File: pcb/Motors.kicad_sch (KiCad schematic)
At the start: 10 parts, among them M1 LEFT, M2 RIGHT, U11 TB6612FNG

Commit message: [pcb] Test points reduced to 1.5mm; flow control series resistors added
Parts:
- TP14, TP15: footprint TestPoint:TestPoint_Pad_D2.0mm -> TestPoint:TestPoint_Pad_D1.5mm
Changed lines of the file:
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@@
       (effects (font (size 1.27 1.27)) (justify left) hide)
     )
-    (property "Footprint" "TestPoint:TestPoint_Pad_D2.0mm" (at 30.48 68.58 0)
+    (property "Footprint" "TestPoint:TestPoint_Pad_D1.5mm" (at 30.48 68.58 0)
       (effects (font (size 1.27 1.27)) hide)
     )
@@
       (effects (font (size 1.27 1.27)) (justify left) hide)
     )
-    (property "Footprint" "TestPoint:TestPoint_Pad_D2.0mm" (at 40.64 63.5 0)
+    (property "Footprint" "TestPoint:TestPoint_Pad_D1.5mm" (at 40.64 63.5 0)
       (effects (font (size 1.27 1.27)) hide)
     )
@@
   (symbol (lib_id "power:+3.3V") (at 46.99 58.42 0) (unit 1)
     (in_bom yes) (on_board yes) (dnp no) (fields_autoplaced)
-    (property "Reference" "#PWR041" (at 46.99 62.23 0)
+    (property "Reference" "#PWR054" (at 46.99 62.23 0)
       (effects (font (size 1.27 1.27)) hide)
     )
@@
       (project "Autko"
         (path "/8d5cfdec-de34-4148-9100-7125640c46f5/541574ca-21e4-445f-b8e2-ded2c59d3b8a"
-          (reference "#PWR041") (unit 1)
+          (reference "#PWR054") (unit 1)
         )
       )
@@
   (symbol (lib_id "power:GND") (at 90.17 44.45 0) (unit 1)
     (in_bom yes) (on_board yes) (dnp no)
-    (property "Reference" "#PWR040" (at 90.17 50.8 0)
+    (property "Reference" "#PWR053" (at 90.17 50.8 0)
       (effects (font (size 1.27 1.27)) hide)
     )
@@
       (project "Autko"
         (path "/8d5cfdec-de34-4148-9100-7125640c46f5/541574ca-21e4-445f-b8e2-ded2c59d3b8a"
-          (reference "#PWR040") (unit 1)
+          (reference "#PWR053") (unit 1)
         )
       )
@@
   (symbol (lib_id "power:+3.3V") (at 46.99 31.75 0) (unit 1)
     (in_bom yes) (on_board yes) (dnp no) (fields_autoplaced)
-    (property "Reference" "#PWR037" (at 46.99 35.56 0)
+    (property "Reference" "#PWR050" (at 46.99 35.56 0)
       (effects (font (size 1.27 1.27)) hide)
     )
@@
       (project "Autko"
         (path "/8d5cfdec-de34-4148-9100-7125640c46f5/541574ca-21e4-445f-b8e2-ded2c59d3b8a"
-          (reference "#PWR037") (unit 1)
+          (reference "#PWR050") (unit 1)
         )
       )
@@
   (symbol (lib_id "power:+7.5V") (at 90.17 31.75 0) (unit 1)
     (in_bom yes) (on_board yes) (dnp no) (fields_autoplaced)
-    (property "Reference" "#PWR038" (at 90.17 35.56 0)
+    (property "Reference" "#PWR051" (at 90.17 35.56 0)
       (effects (font (size 1.27 1.27)) hide)
     )
@@
       (project "Autko"
         (path "/8d5cfdec-de34-4148-9100-7125640c46f5/541574ca-21e4-445f-b8e2-ded2c59d3b8a"
-          (reference "#PWR038") (unit 1)
+          (reference "#PWR051") (unit 1)
         )
       )
@@
   (symbol (lib_id "power:GND") (at 46.99 44.45 0) (unit 1)
     (in_bom yes) (on_board yes) (dnp no)
-    (property "Reference" "#PWR039" (at 46.99 50.8 0)
+    (property "Reference" "#PWR052" (at 46.99 50.8 0)
       (effects (font (size 1.27 1.27)) hide)
     )
@@
       (project "Autko"
         (path "/8d5cfdec-de34-4148-9100-7125640c46f5/541574ca-21e4-445f-b8e2-ded2c59d3b8a"
-          (reference "#PWR039") (unit 1)
+          (reference "#PWR052") (unit 1)
         )
       )
@@
   (symbol (lib_id "power:GND") (at 67.31 97.79 0) (unit 1)
     (in_bom yes) (on_board yes) (dnp no)
-    (property "Reference" "#PWR042" (at 67.31 104.14 0)
+    (property "Reference" "#PWR055" (at 67.31 104.14 0)
       (effects (font (size 1.27 1.27)) hide)
     )
@@
       (project "Autko"
         (path "/8d5cfdec-de34-4148-9100-7125640c46f5/541574ca-21e4-445f-b8e2-ded2c59d3b8a"
-          (reference "#PWR042") (unit 1)
-        )
-      )
+          (reference "#PWR055") (unit 1)
+        )
+      )

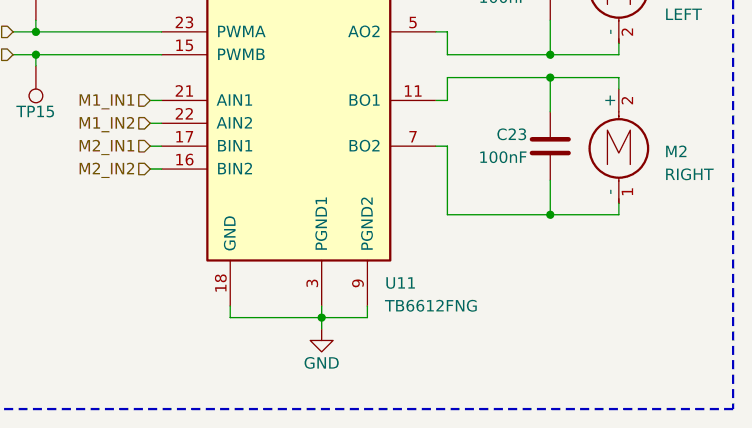
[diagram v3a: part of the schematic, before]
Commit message: [pcb] Rename line sensors to S1..S7
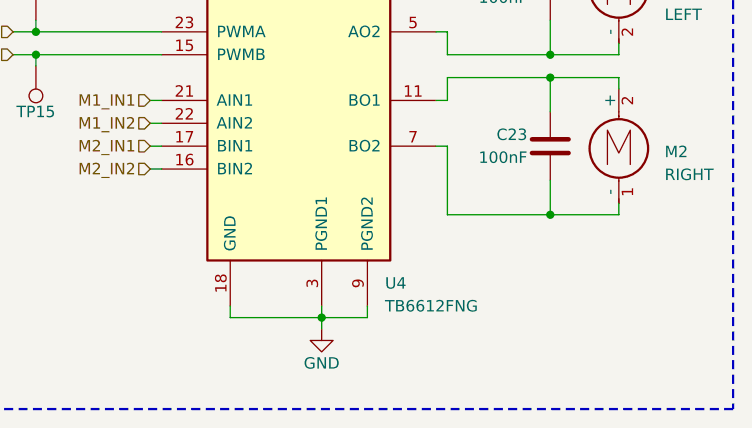
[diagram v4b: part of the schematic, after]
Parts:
- renumbered U11 to U4
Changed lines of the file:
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@@
   (symbol (lib_id "Driver_Motor:TB6612FNG") (at 64.77 69.85 0) (unit 1)
     (in_bom yes) (on_board yes) (dnp no) (fields_autoplaced)
-    (property "Reference" "U11" (at 74.3459 92.71 0)
+    (property "Reference" "U4" (at 74.3459 92.71 0)
       (effects (font (size 1.27 1.27)) (justify left))
     )
@@
       (project "Autko"
         (path "/8d5cfdec-de34-4148-9100-7125640c46f5/541574ca-21e4-445f-b8e2-ded2c59d3b8a"
-          (reference "U11") (unit 1)
+          (reference "U4") (unit 1)
         )
       )

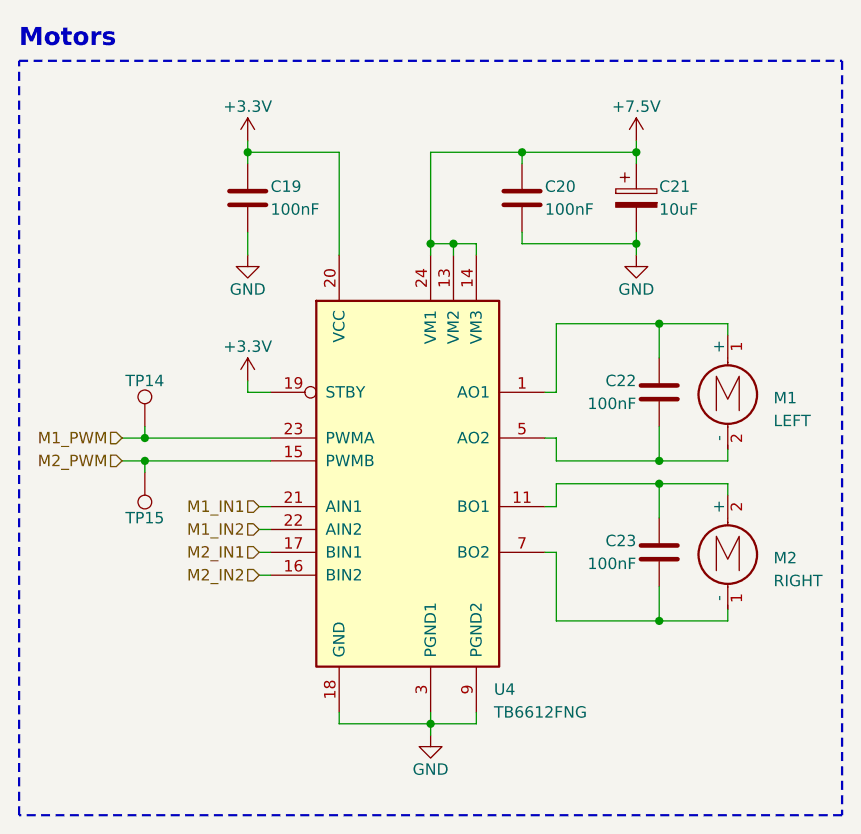
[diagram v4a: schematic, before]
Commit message: [pcb] Assign smaller footprints
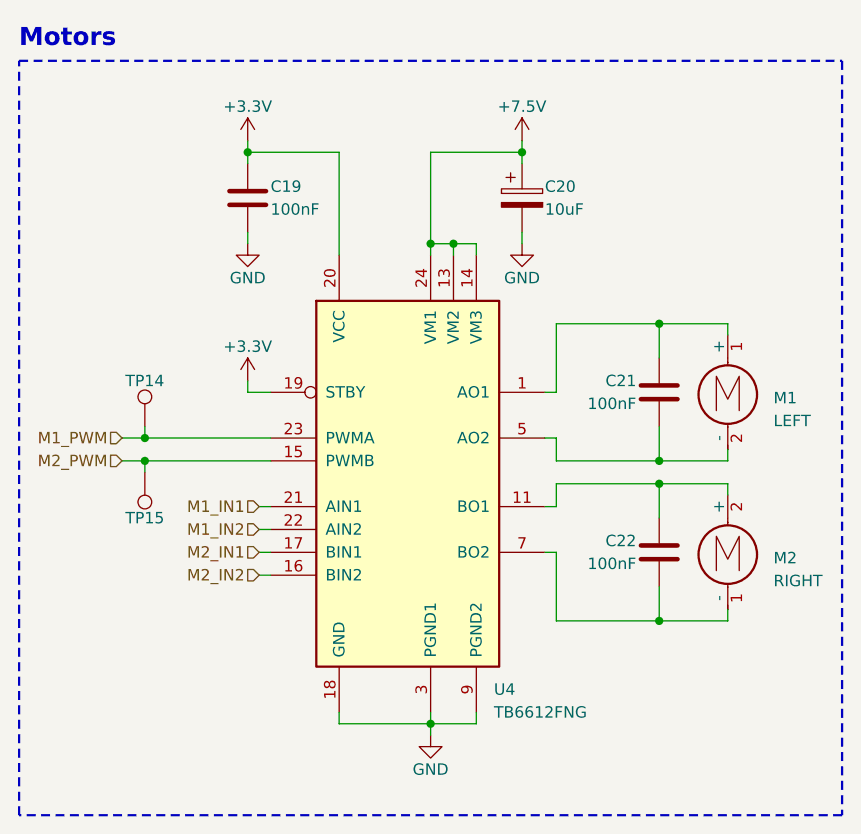
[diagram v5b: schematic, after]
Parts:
- removed C20: 100nF, Capacitor_SMD:C_0805_2012Metric, symbol Device:C
- C19: footprint Capacitor_SMD:C_0805_2012Metric -> Capacitor_SMD:C_0603_1608Metric
- C20: renamed from C21; footprint Capacitor_Tantalum_SMD:CP_EIA-3528-12_Kemet-T -> Capacitor_SMD:C_1206_3216Metric
- C21: renamed from C22; footprint Capacitor_SMD:C_0805_2012Metric -> Capacitor_SMD:C_0603_1608Metric
- C22: renamed from C23; footprint Capacitor_SMD:C_0805_2012Metric -> Capacitor_SMD:C_0603_1608Metric
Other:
- moved on the sheet: C20
